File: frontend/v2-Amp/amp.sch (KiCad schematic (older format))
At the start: 72 parts, among them K1 HK4100, P1 Antenna, P2 CONN_02X06, P3 TX Power Tap, P4 TX-IN, P5 RX IN, P6 12-13.8v, Q1 PZT2222A, Q2 RD16HHF1, T1 OUT_TRANSF, T2 BN-43-2402, U1 LP2951-50D

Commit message: v2rx changes and update to new kicad
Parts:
- C1, C10, C11, C12, C13, C15, C16, C17, C18, C19, C2, C3, C4, C5, C6, C63, C64, C65, C66, C67, C68, C69, C7, C8, C84, C85, C86, C87, C88, C89, C9: symbol C -> C-RESCUE-amp
- C14, C20: symbol CP1 -> CP1-RESCUE-amp
- R1, R10, R11, R12, R13, R14, R15, R16, R17, R18, R19, R2, R26, R27, R28, R3, R4, R5, R6, R7, R8, R9: symbol R -> R-RESCUE-amp

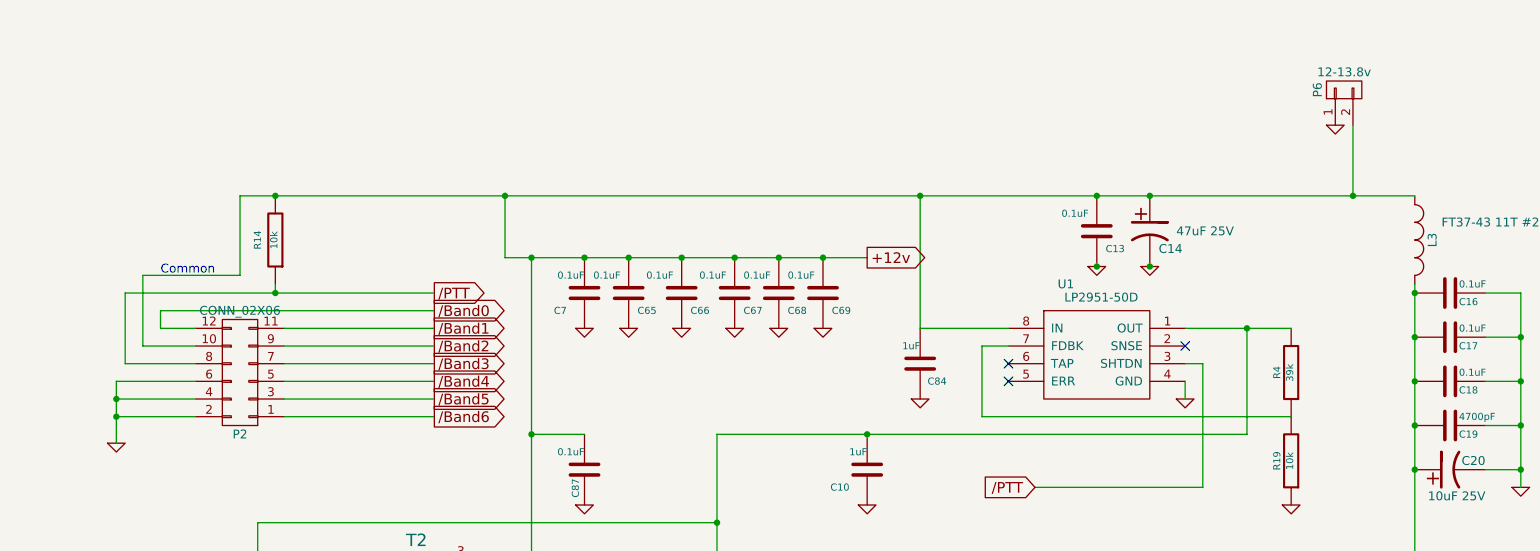
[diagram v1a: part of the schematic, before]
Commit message: Updates for v1.1 amp and V1.4 ADC
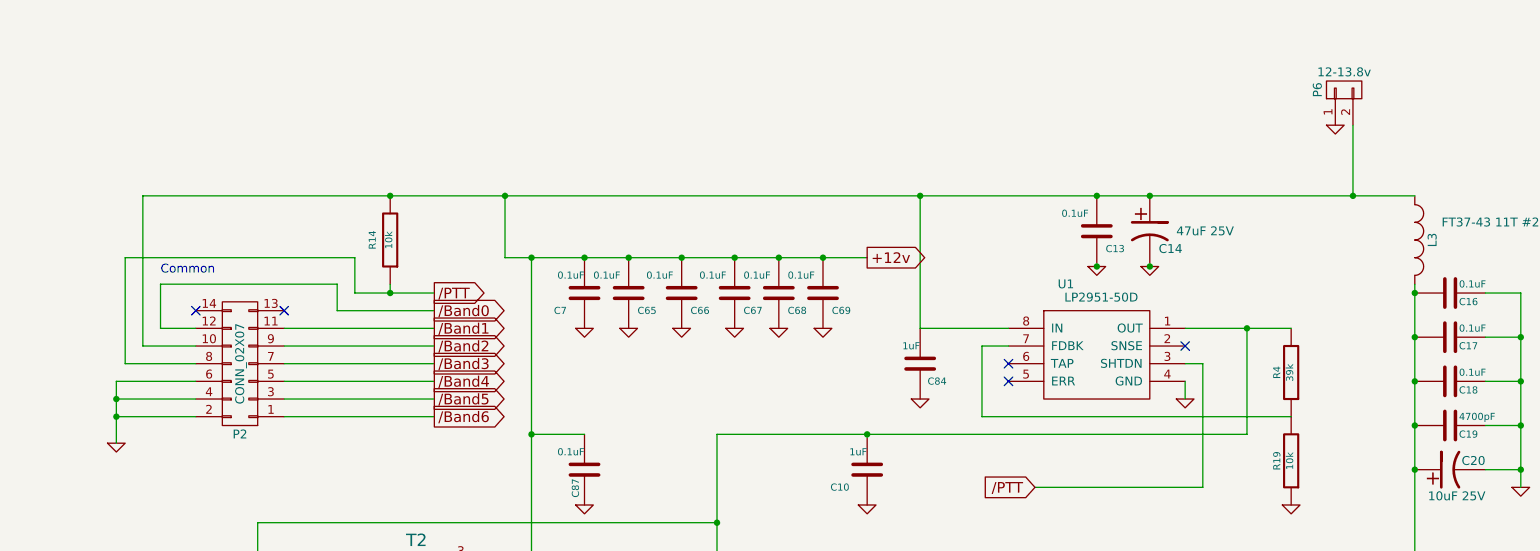
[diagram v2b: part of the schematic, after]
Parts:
- removed P2: CONN_02X06, Pin_Headers:Pin_Header_Angled_2x06, symbol CONN_02X06
- added P2: CONN_02X07, Pin_Headers:Pin_Header_Straight_2x07, symbol CONN_02X07
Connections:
- net +12v: now also P2.10 (P10)
- net /Band0: now also P2.12 (P12)
- net /Band1: now also P2.11 (P11)
- net /Band2: now also P2.9 (P9)
- net /Band3: now also P2.7 (P7)
- net /Band4: now also P2.5 (P5)
- net /Band5: now also P2.3 (P3)
- net /Band6: now also P2.1 (P1)
- net /PTT: now also P2.8 (P8)
- net GND: now also P2.2 (P2), P2.4 (P4), P2.6 (P6)
- no-connect marks 5 -> 7
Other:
- moved on the sheet: R14
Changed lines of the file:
@@
 Connection ~ 9400 2050
 Wire Wire Line
-	8450 850  8450 1250
+	8450 1250 8450 850
 Connection ~ 8450 1250
 Wire Wire Line
@@
 Hi-Z\nTap
 Connection ~ 5700 2600
-Wire Wire Line
-	2350 1750 2350 1800
-Connection ~ 2350 1800
 $Comp
 L C-RESCUE-amp C66
@@
 L R-RESCUE-amp R14
 U 1 1 55E09ECA
-P 2350 1500
-F 0 "R14" V 2450 1500 40  0000 C CNN
-F 1 "10k" V 2357 1501 40  0000 C CNN
-F 2 "Resistors_SMD:R_0805_HandSoldering" V 2280 1500 30  0001 C CNN
-F 3 "" H 2350 1500 30  0000 C CNN
-	1    2350 1500
-	-1   0    0    1
-$EndComp
-Wire Wire Line
-	2150 1700 2150 1250
-Connection ~ 2350 1250
+P 3000 1500
+F 0 "R14" V 3100 1500 40  0000 C CNN
+F 1 "10k" V 3007 1501 40  0000 C CNN
+F 2 "Resistors_SMD:R_0805_HandSoldering" V 2930 1500 30  0001 C CNN
+F 3 "" H 3000 1500 30  0000 C CNN
+	1    3000 1500
+	-1   0    0    1
+$EndComp
 Wire Wire Line
 	3650 1600 5700 1600
@@
 $EndComp
 Wire Wire Line
-	2150 1250 8800 1250
+	1600 1250 8800 1250
 $Comp
 L R-RESCUE-amp R9
@@
 	1600 2100 1900 2100
 Wire Wire Line
-	1600 2100 1600 1700
-Wire Wire Line
-	1600 1700 2150 1700
-Wire Wire Line
-	3250 1800 1500 1800
-Wire Wire Line
-	1500 1800 1500 2200
+	1600 1250 1600 2100
+Wire Wire Line
+	1500 1600 1500 2200
 Wire Wire Line
 	1500 2200 1900 2200
@@
 	1450 2300 1450 2650
 Wire Wire Line
-	1700 2000 1700 1900
-Wire Wire Line
-	1700 1900 3250 1900
+	1700 1750 1700 2000
 Connection ~ 1450 2400
-$Comp
-L CONN_02X06 P2
-U 1 1 55E5C678
-P 2150 2250
-F 0 "P2" H 2150 2600 50  0000 C CNN
-F 1 "CONN_02X06" H 2150 1900 50  0000 C CNN
-F 2 "Pin_Headers:Pin_Header_Angled_2x06" H 2150 1050 60  0001 C CNN
-F 3 "" H 2150 1050 60  0000 C CNN
-	1    2150 2250
-	-1   0    0    1
-$EndComp
 Wire Wire Line
 	1700 2000 1900 2000
@@
 NoConn ~ 7500 2100
 NoConn ~ 6500 2200
+$Comp
+L CONN_02X07 P2
+U 1 1 56B8B30D
+P 2150 2200
+F 0 "P2" H 2150 2600 50  0000 C CNN
+F 1 "CONN_02X07" V 2150 2200 50  0000 C CNN
+F 2 "Pin_Headers:Pin_Header_Straight_2x07" H 2150 1000 50  0001 C CNN
+F 3 "" H 2150 1000 50  0000 C CNN
+	1    2150 2200
+	-1   0    0    1
+$EndComp
+Connection ~ 3000 1250
+Wire Wire Line
+	1500 1600 2800 1600
+Wire Wire Line
+	2800 1600 2800 1800
+Wire Wire Line
+	2800 1800 3250 1800
+Wire Wire Line
+	3000 1750 3000 1800
+Connection ~ 3000 1800
+Wire Wire Line
+	1700 1750 2700 1750
+Wire Wire Line
+	2700 1750 2700 1900
+Wire Wire Line
+	2700 1900 3250 1900
+NoConn ~ 2400 1900
+NoConn ~ 1900 1900
 $EndSCHEMATC

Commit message: Ver 1.1 changes
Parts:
- removed C12, C85, C87: 0.1uF, HERMESLITE:C_0805, symbol C-RESCUE-amp
- removed C2: 82pf, HERMESLITE:C_0805, symbol C-RESCUE-amp
- removed C3, C63: DNI, HERMESLITE:C_0805, symbol C-RESCUE-amp
- removed C4, C6: 150pf, HERMESLITE:C_0805, symbol C-RESCUE-amp
- removed C5: 56pf, HERMESLITE:C_0805, symbol C-RESCUE-amp
- removed C64: 82pF, HERMESLITE:C_0805, symbol C-RESCUE-amp
- removed L1, L22: 363nH, HERMESLITE:Choke_Toroid, symbol INDUCTOR
- removed L2: 243nH, HERMESLITE:Choke_Toroid, symbol INDUCTOR
- removed Q1: PZT2222A, TO_SOT_Packages_SMD:SOT-223, symbol PZT2222A-T
- removed R11: 1k, Resistors_SMD:R_0805_HandSoldering, symbol R-RESCUE-amp
- removed R13: 4.7, Resistors_SMD:R_0805_HandSoldering, symbol R-RESCUE-amp
- removed R18: 47, Resistors_SMD:R_0805_HandSoldering, symbol R-RESCUE-amp
- removed R9: 1.2k, Resistors_SMD:R_0805_HandSoldering, symbol R-RESCUE-amp
- removed T2: BN-43-2402, HERMESLITE:TRANSF, symbol TRANSFO2
- added L23: 100nH, Resistors_SMD:R_0805_HandSoldering, symbol INDUCTOR_SMALL
- Q2: footprint Transistors_TO-220:TO-220_Neutral123_Vertical -> TO_SOT_Packages_THT:TO-220_Neutral123_Vertical
- R10: value 18 -> 0
- R12, R8: value 270 -> DNI
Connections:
- net at C11.2, R15.1, R16.1: now also L23.1; no longer Q2.1 (G)
- net at C1.2, R1.2: now also K1.3
- net at P4.2 (P2): now also C86.1
- new net: L23.2, Q2.1 (G)
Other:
- note added: "Optional Attenuator Pad\n"
- note removed: "1T #30\n"
- note removed: "30MHz low pass for RX and 10/12M LPF for TX"
- note removed: "3T #30\n"
- note removed: "5T #30\n"
- note removed: "8T T37-6\n6in #26"
- note removed: "9T T37-6\n7in #26"
- note removed: "Attenuator (3db example) needed \nto ensure that input impedance\nof Norton amplifier is 50 ohms."
- note removed: "Microstrip\nW=15Mil L=1800Mil"
- moved on the sheet: P4

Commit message: Updates for v1.1
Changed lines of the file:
@@
 Wire Wire Line
 	6450 4200 6500 4200
+Connection ~ 6450 4200
+Connection ~ 6500 4200
+Connection ~ 5950 4200
+Connection ~ 5900 4200
 $EndSCHEMATC
